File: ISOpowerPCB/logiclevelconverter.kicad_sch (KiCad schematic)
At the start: 6 parts

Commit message: PCB Notes added
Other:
- note added: "NOTE: REPLACE WITH THIS."
- note added: "https://www.ti.com/lit/ds/symlink/txs0104e.pdf?ts=1643186590728&ref_url=https%253A%252F%252Fwww.ti.com%252Fproduct%252FTXS0104E%253FkeyMatch%253D%2526tisearch%253Dsearch-everything%2526usecase%253Dpartmatches"
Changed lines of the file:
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@@
     (stroke (width 0) (type default) (color 0 0 0 0))
+  )
+  (text "https://www.ti.com/lit/ds/symlink/txs0104e.pdf?ts=1643186590728&ref_url=https%253A%252F%252Fwww.ti.com%252Fproduct%252FTXS0104E%253FkeyMatch%253D%2526tisearch%253Dsearch-everything%2526usecase%253Dpartmatches"
+    (at 29.21 135.89 0)
+    (effects (font (size 1.27 1.27)) (justify left bottom))
+  )
+  (text "NOTE: REPLACE WITH THIS." (at 30.48 133.35 0)
+    (effects (font (size 1.27 1.27)) (justify left bottom))
   )
   (global_label "V_A" (shape input) (at 64.77 66.04 90) (fields_autoplaced)

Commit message: significant changes
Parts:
- removed Q? (x2): BSS138, Package_TO_SOT_SMD:SOT-23, symbol Transistor_FET:BSS138
- removed R? (x4): 10k, Resistor_SMD:R_0805_2012Metric_Pad1.20x1.40mm_HandSolder, symbol 000_Resistors_Immo:Resistor_0805
- added C? (x2): 100n, Capacitor_SMD:C_0805_2012Metric_Pad1.18x1.45mm_HandSolder, symbol 000_Capacitor_film_immo:cap_film_0805
- added R?: 10k, Resistor_SMD:R_0805_2012Metric_Pad1.20x1.40mm_HandSolder, symbol 000_Resistors_Immo:Resistor_0805
- added U?: TXS0102DCT, Package_SO:SSOP-8_2.95x2.8mm_P0.65mm, symbol Logic_LevelTranslator:TXS0102DCT
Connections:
- net 0A: now also U?.5 (A1)
- net 0B: now also U?.8 (B1)
- net 1A: now also U?.4 (A2)
- net 1B: now also U?.1 (B2)
- new net 3V3_IN: C?.1, U?.3 (VCCA)
- new net 5V_IN: C?.1, U?.7 (VCCB)
- new net GND: C?.2, C?.2, R?.2, U?.2 (GND)
- new net OE: R?.1, U?.6 (OE)
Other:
- note added: "Keep OE LOW until VccA & VccB are fully ramped & stable"
- note removed: "NOTE: REPLACE WITH THIS."
- note removed: "https://www.ti.com/lit/ds/symlink/txs0104e.pdf?ts=1643186590728&ref_url=https%253A%252F%252Fwww.ti.com%252Fproduct%252FTXS0104E%253FkeyMatch%253D%2526tisearch%253Dsearch-everything%2526usecase%253Dpartmatches"

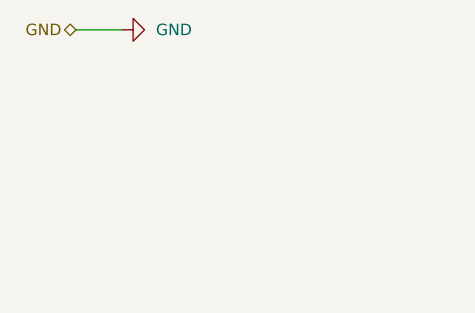
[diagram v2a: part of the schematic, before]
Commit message: Updated as per discussions 26/01/22
# Change Notes

04/02/2022
As per discussion 26/01/22
1. Changed per channel 5v MOSFET switches to MOSFET control of DC/DC module on/off pin - due to failure of MOSFET switching during testing.
2. Added 5v buck converter for independent MCU_5V power bus.
	- Ensured all 5v MCU hardware is powered from common MCU_5V bus.
3. Removed circuit from NC pins on DC/DC modules.
4. Changed ESP32 USB interface to CH340
5. Changed MCU serial logic level converters from MOSFET to IC - TXS0102DCT
	- TODO: OE pin now requires low signal untill DC/DC supply is stable - Does it? Can it just be tied to 5v bus with a large capacitor? Does it need MCU to hold pin low untill 5V_BUS is stable?
6. Removed redundent 3V3_IN to power distribution page.
	- Rechecked all sheets for redundent pins, it won't impact drawing traces, but it will impact readability.
7. Added Mechanical layer as hirarchical sheet.
8. Moved voltage monitoring circuits to hirarchical sheet
9. Added voltage monitoring with TL431DBZ to 12V_BUS
10. Automatic shutoff circuit removed, as this would prevent the DC/DC module from powering on. Instead moved to AtMega328p digital inputs
and microcontroller will control shutdown of DC/DC supply if out of spec voltage detected.
		- This is a severe limitation compared to the specification, and this also does not prevent damage to devices on 5V_BUS if voltage is pulled high, for example to 12v due to user error.
		- TODO: Add independent overvoltage protection to 5V_BUS? 		[Zener Diode Overvoltage Protection - Sparkfun](https://www.rs-online.com/designspark/how-does-zener-diode-do-overvoltage-protection-in-circuit#:~:text=In%20order%20to%20protect%20the,flow%20in%20the%20reverse%20direction).
11. Changed logic level conversion for 12v outputs to 12v drive circuit. [12v drive circuit](https://forum.arduino.cc/t/easiest-way-of-driving-amplifying-from-5v-to-12v/123290)
12. Added proto pin connections for ESP MCU.
13. Changed 20v Zener in reverse vol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
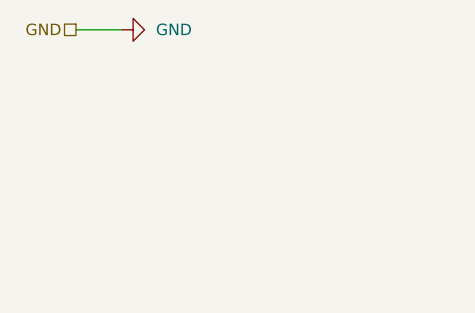
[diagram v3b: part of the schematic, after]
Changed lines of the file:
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@@
     (effects (font (size 0.8 0.8)) (justify left bottom))
   )
-  (hierarchical_label "GND" (shape bidirectional) (at 22.86 17.78 180)
+  (hierarchical_label "GND" (shape passive) (at 22.86 17.78 180)
     (effects (font (size 1.27 1.27)) (justify right))
   )

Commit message: messing around with libraries
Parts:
- C26, C27: renamed from C?; symbol 000_Capacitor_film_immo:cap_film_0805 -> 000_Capacitor_FIlm_Immo:cap_film_0805
- gave numbers to parts that had none: 2
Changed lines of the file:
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@@
     (effects (font (size 1.27 1.27)) (justify left))
   )
-  (symbol (lib_id "000_Capacitor_film_immo:cap_film_0805") (at 167.64 96.52 0) (unit 1)
+  (symbol (lib_id "000_Capacitor_FIlm_Immo:cap_film_0805") (at 167.64 96.52 0) (unit 1)
     (in_bom yes) (on_board yes) (fields_autoplaced)
-    (property "Reference" "C?" (id 0) (at 171.45 95.2499 0)
+    (property "Reference" "C27" (id 0) (at 171.45 95.2499 0)
       (effects (font (size 1.27 1.27)) (justify left))
     )
@@
     (pin "2")
   )
-  (symbol (lib_id "000_Capacitor_film_immo:cap_film_0805") (at 115.57 96.52 0) (unit 1)
+  (symbol (lib_id "000_Capacitor_FIlm_Immo:cap_film_0805") (at 115.57 96.52 0) (unit 1)
     (in_bom yes) (on_board yes) (fields_autoplaced)
-    (property "Reference" "C?" (id 0) (at 119.38 95.2499 0)
+    (property "Reference" "C26" (id 0) (at 119.38 95.2499 0)
       (effects (font (size 1.27 1.27)) (justify left))
     )
@@
   (symbol (lib_id "power:GND") (at 143.51 116.84 0) (unit 1)
     (in_bom yes) (on_board yes) (fields_autoplaced)
-    (property "Reference" "#PWR?" (id 0) (at 143.51 123.19 0)
+    (property "Reference" "#PWR081" (id 0) (at 143.51 123.19 0)
       (effects (font (size 1.27 1.27)) hide)
     )
@@
   (symbol (lib_id "power:GND") (at 27.94 17.78 90) (unit 1)
     (in_bom yes) (on_board yes) (fields_autoplaced)
-    (property "Reference" "#PWR?" (id 0) (at 34.29 17.78 0)
+    (property "Reference" "#PWR080" (id 0) (at 34.29 17.78 0)
       (effects (font (size 1.27 1.27)) hide)
     )
@@
   (symbol (lib_id "000_Resistors_Immo:Resistor_0805") (at 128.27 107.95 0) (unit 1)
     (in_bom yes) (on_board yes) (fields_autoplaced)
-    (property "Reference" "R?" (id 0) (at 130.81 106.6799 0)
+    (property "Reference" "R24" (id 0) (at 130.81 106.6799 0)
       (effects (font (size 1.27 1.27)) (justify left))
     )
@@
   (symbol (lib_id "Logic_LevelTranslator:TXS0102DCT") (at 143.51 95.25 0) (unit 1)
     (in_bom yes) (on_board yes) (fields_autoplaced)
-    (property "Reference" "U?" (id 0) (at 145.5294 107.95 0)
+    (property "Reference" "U13" (id 0) (at 145.5294 107.95 0)
       (effects (font (size 1.27 1.27)) (justify left))
     )

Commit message: fixed most electrical rules check violations
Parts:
- C26, C27: symbol 000_Capacitor_FIlm_Immo:cap_film_0805 -> 000_Capacitor_Film_Immo:cap_film_0805
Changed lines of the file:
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@@
     (effects (font (size 1.27 1.27)) (justify left))
   )
-  (symbol (lib_id "000_Capacitor_FIlm_Immo:cap_film_0805") (at 167.64 96.52 0) (unit 1)
+  (symbol (lib_id "000_Capacitor_Film_Immo:cap_film_0805") (at 167.64 96.52 0) (unit 1)
     (in_bom yes) (on_board yes) (fields_autoplaced)
     (property "Reference" "C27" (id 0) (at 171.45 95.2499 0)
@@
     (pin "2")
   )
-  (symbol (lib_id "000_Capacitor_FIlm_Immo:cap_film_0805") (at 115.57 96.52 0) (unit 1)
+  (symbol (lib_id "000_Capacitor_Film_Immo:cap_film_0805") (at 115.57 96.52 0) (unit 1)
     (in_bom yes) (on_board yes) (fields_autoplaced)
     (property "Reference" "C26" (id 0) (at 119.38 95.2499 0)

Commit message: Footprint Associations 50% complete
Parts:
- added C31: 100u, Capacitor_SMD:CP_Elec_6.3x7.7, symbol 000_Capacitor_Electrolytic_Immo:100u
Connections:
- net OE is gone; now on net 3V3_IN: R24.1, U13.6 (OE)
- net 3V3_IN: now also C31.1
- net GND: now also C31.2
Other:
- moved on the sheet: C26
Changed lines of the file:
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@@
   (junction (at 146.05 81.28) (diameter 0) (color 0 0 0 0)
   )
+  (junction (at 119.38 102.87) (diameter 0) (color 0 0 0 0)
+  )
+  (junction (at 119.38 81.28) (diameter 0) (color 0 0 0 0)
+  )
+  (junction (at 143.51 113.03) (diameter 0) (color 0 0 0 0)
+  )
+  (junction (at 128.27 113.03) (diameter 0) (color 0 0 0 0)
+  )
   (junction (at 128.27 102.87) (diameter 0) (color 0 0 0 0)
   )
-  (junction (at 143.51 113.03) (diameter 0) (color 0 0 0 0)
-  )
-  (junction (at 128.27 113.03) (diameter 0) (color 0 0 0 0)
-  )
   (junction (at 140.97 81.28) (diameter 0) (color 0 0 0 0)
   )
+  (junction (at 119.38 113.03) (diameter 0) (color 0 0 0 0)
+  )
   (wire (pts (xy 129.54 92.71) (xy 133.35 92.71))
     (stroke (width 0) (type default) (color 0 0 0 0))
   )
+  (wire (pts (xy 119.38 113.03) (xy 128.27 113.03))
+    (stroke (width 0) (type default) (color 0 0 0 0))
+  )
   (wire (pts (xy 143.51 113.03) (xy 143.51 116.84))
     (stroke (width 0) (type default) (color 0 0 0 0))
@@
     (stroke (width 0) (type default) (color 0 0 0 0))
   )
-  (wire (pts (xy 116.84 102.87) (xy 116.84 101.6))
+  (wire (pts (xy 119.38 102.87) (xy 119.38 104.14))
     (stroke (width 0) (type default) (color 0 0 0 0))
   )
@@
     (stroke (width 0) (type default) (color 0 0 0 0))
   )
-  (wire (pts (xy 140.97 81.28) (xy 115.57 81.28))
+  (wire (pts (xy 140.97 81.28) (xy 119.38 81.28))
+    (stroke (width 0) (type default) (color 0 0 0 0))
+  )
+  (wire (pts (xy 128.27 102.87) (xy 119.38 102.87))
     (stroke (width 0) (type default) (color 0 0 0 0))
   )
@@
     (stroke (width 0) (type default) (color 0 0 0 0))
   )
-  (wire (pts (xy 115.57 81.28) (xy 115.57 92.71))
+  (wire (pts (xy 106.68 81.28) (xy 106.68 92.71))
     (stroke (width 0) (type default) (color 0 0 0 0))
   )
@@
     (stroke (width 0) (type default) (color 0 0 0 0))
   )
-  (wire (pts (xy 116.84 101.6) (xy 114.3 101.6))
-    (stroke (width 0) (type default) (color 0 0 0 0))
-  )
   (wire (pts (xy 146.05 81.28) (xy 146.05 82.55))
     (stroke (width 0) (type default) (color 0 0 0 0))
   )
+  (wire (pts (xy 106.68 100.33) (xy 106.68 113.03))
+    (stroke (width 0) (type default) (color 0 0 0 0))
+  )
   (wire (pts (xy 157.48 97.79) (xy 153.67 97.79))
     (stroke (width 0) (type default) (color 0 0 0 0))
   )
-  (wire (pts (xy 115.57 113.03) (xy 128.27 113.03))
-    (stroke (width 0) (type default) (color 0 0 0 0))
-  )
-  (wire (pts (xy 116.84 102.87) (xy 128.27 102.87))
+  (wire (pts (xy 119.38 111.76) (xy 119.38 113.03))
+    (stroke (width 0) (type default) (color 0 0 0 0))
+  )
+  (wire (pts (xy 119.38 81.28) (xy 106.68 81.28))
+    (stroke (width 0) (type default) (color 0 0 0 0))
+  )
+  (wire (pts (xy 106.68 113.03) (xy 119.38 113.03))
     (stroke (width 0) (type default) (color 0 0 0 0))
   )
@@
     (stroke (width 0) (type default) (color 0 0 0 0))
   )
+  (wire (pts (xy 119.38 102.87) (xy 119.38 81.28))
+    (stroke (width 0) (type default) (color 0 0 0 0))
+  )
   (wire (pts (xy 140.97 73.66) (xy 140.97 81.28))
     (stroke (width 0) (type default) (color 0 0 0 0))
   )
   (wire (pts (xy 167.64 81.28) (xy 167.64 92.71))
-    (stroke (width 0) (type default) (color 0 0 0 0))
-  )
-  (wire (pts (xy 115.57 100.33) (xy 115.57 113.03))
-    (stroke (width 0) (type default) (color 0 0 0 0))
-  )
-  (wire (pts (xy 114.3 101.6) (xy 114.3 102.87))
-    (stroke (width 0) (type default) (color 0 0 0 0))
-  )
-  (wire (pts (xy 85.09 102.87) (xy 114.3 102.87))
     (stroke (width 0) (type default) (color 0 0 0 0))
   )
@@
     (effects (font (size 1.27 1.27)) (justify right))
   )
-  (hierarchical_label "OE" (shape input) (at 85.09 102.87 180)
-    (effects (font (size 1.27 1.27)) (justify right))
-  )
   (hierarchical_label "1A" (shape bidirectional) (at 129.54 97.79 180)
     (effects (font (size 1.27 1.27)) (justify right))
@@
     (pin "2")
   )
-  (symbol (lib_id "000_Capacitor_Film_Immo:cap_film_0805") (at 115.57 96.52 0) (unit 1)
-    (in_bom yes) (on_board yes) (fields_autoplaced)
-    (property "Reference" "C26" (id 0) (at 119.38 95.2499 0)
-      (effects (font (size 1.27 1.27)) (justify left))
-    )
-    (property "Value" "100n" (id 1) (at 119.38 97.7899 0)
-      (effects (font (size 1.27 1.27)) (justify left))
-    )
-    (property "Footprint" "Capacitor_SMD:C_0805_2012Metric_Pad1.18x1.45mm_HandSolder" (id 2) (at 116.84 106.68 0)
-      (effects (font (size 1.27 1.27)) hide)
-    )
-    (property "Datasheet" "~" (id 3) (at 115.57 96.52 0)
+  (symbol (lib_id "000_Capacitor_Film_Immo:cap_film_0805") (at 106.68 96.52 0) (unit 1)
+    (in_bom yes) (on_board yes) (fields_autoplaced)
+    (property "Reference" "C26" (id 0) (at 110.49 95.2499 0)
+      (effects (font (size 1.27 1.27)) (justify left))
+    )
+    (property "Value" "100n" (id 1) (at 110.49 97.7899 0)
+      (effects (font (size 1.27 1.27)) (justify left))
+    )
+    (property "Footprint" "Capacitor_SMD:C_0805_2012Metric_Pad1.18x1.45mm_HandSolder" (id 2) (at 107.95 106.68 0)
+      (effects (font (size 1.27 1.27)) hide)
+    )
+    (property "Datasheet" "~" (id 3) (at 106.68 96.52 0)
       (effects (font (size 1.27 1.27)) hide)
     )
@@
     (pin "1")
   )
+  (symbol (lib_id "000_Capacitor_Electrolytic_Immo:100u") (at 119.38 107.95 0) (unit 1)
+    (in_bom yes) (on_board yes)
+    (property "Reference" "C31" (id 0) (at 113.03 105.41 0)
+      (effects (font (size 1.27 1.27)) (justify left))
+    )
+    (property "Value" "100u" (id 1) (at 111.76 109.22 0)
+      (effects (font (size 1.27 1.27)) (justify left))
+    )
+    (property "Footprint" "Capacitor_SMD:CP_Elec_6.3x7.7" (id 2) (at 120.3452 111.76 0)
+      (effects (font (size 1.27 1.27)) hide)
+    )
+    (property "Datasheet" "~" (id 3) (at 119.38 107.95 0)
+      (effects (font (size 1.27 1.27)) hide)
+    )
+    (pin "1")
+    (pin "2")
+  )
   (symbol (lib_id "000_Resistors_Immo:Resistor_0805") (at 128.27 107.95 0) (unit 1)
